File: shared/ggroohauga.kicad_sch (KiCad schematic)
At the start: 6 parts

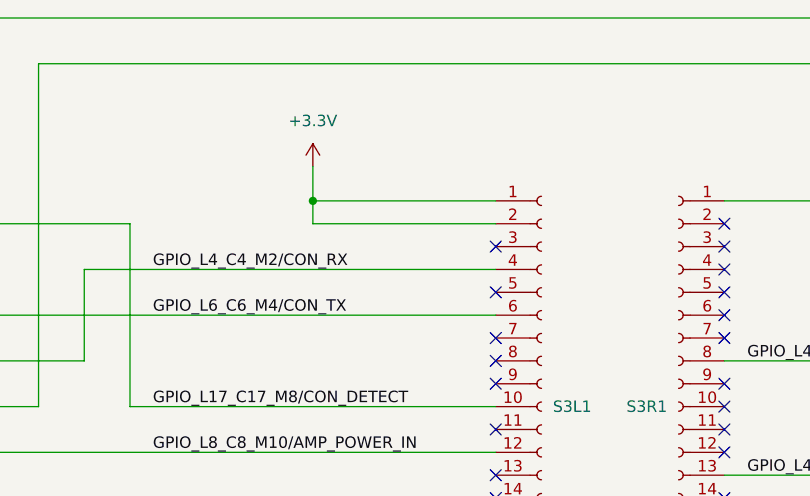
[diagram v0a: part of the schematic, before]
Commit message: Fix compatibility with ESP32-S3-DevKitM-1
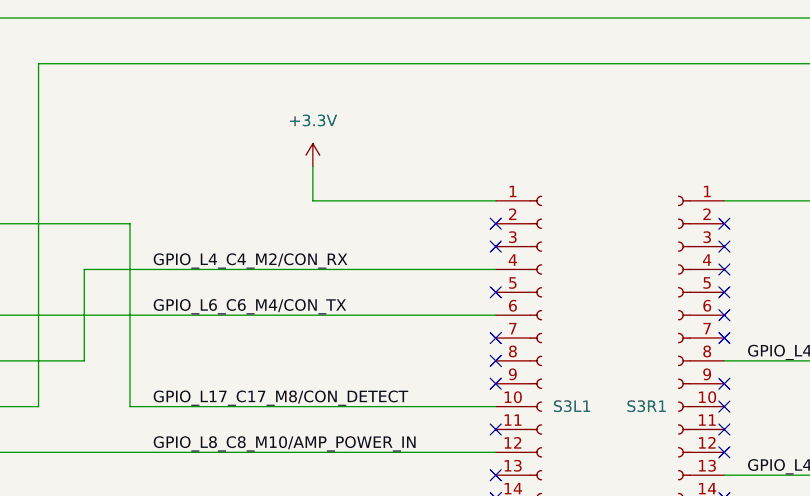
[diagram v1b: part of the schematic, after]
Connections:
- net +3.3V: no longer S3L1.2 (Pin_2)
- no-connect marks 45 -> 46
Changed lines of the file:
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@@
 	(paper "A4")
-	(junction
-		(at 144.78 40.64)
-		(diameter 0)
-		(color 0 0 0 0)
-	)
 	(junction
 		(at 66.04 74.93)
@@
 	)
 	(no_connect
+		(at 165.1 43.18)
+	)
+	(no_connect
 		(at 73.66 129.54)
 	)
@@
 	(wire
 		(pts
-			(xy 165.1 43.18) (xy 144.78 43.18)
-		)
-		(stroke
-			(width 0)
-			(type default)
-		)
-	)
-	(wire
-		(pts
 			(xy 190.5 81.28) (xy 275.59 81.28)
 		)
@@
 		)
 		(stroke
-			(width 0)
-			(type default)
-		)
-	)
-	(wire
-		(pts
-			(xy 144.78 40.64) (xy 144.78 43.18)
-		)
-		(stroke

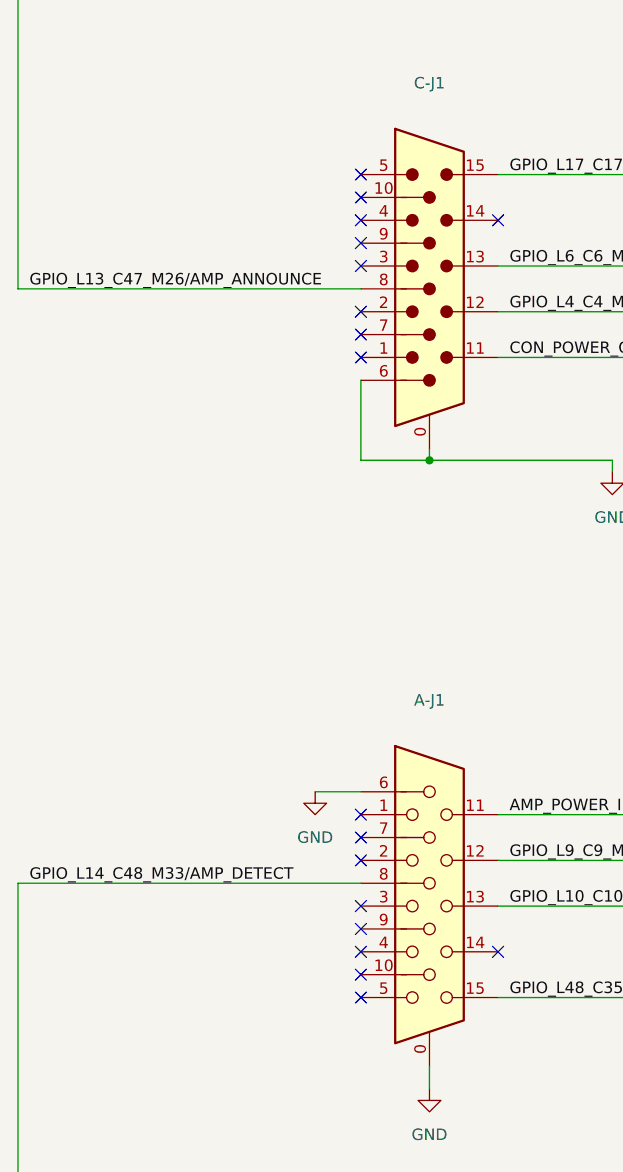
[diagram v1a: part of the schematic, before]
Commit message: Connect audio pins on the bridge PCB
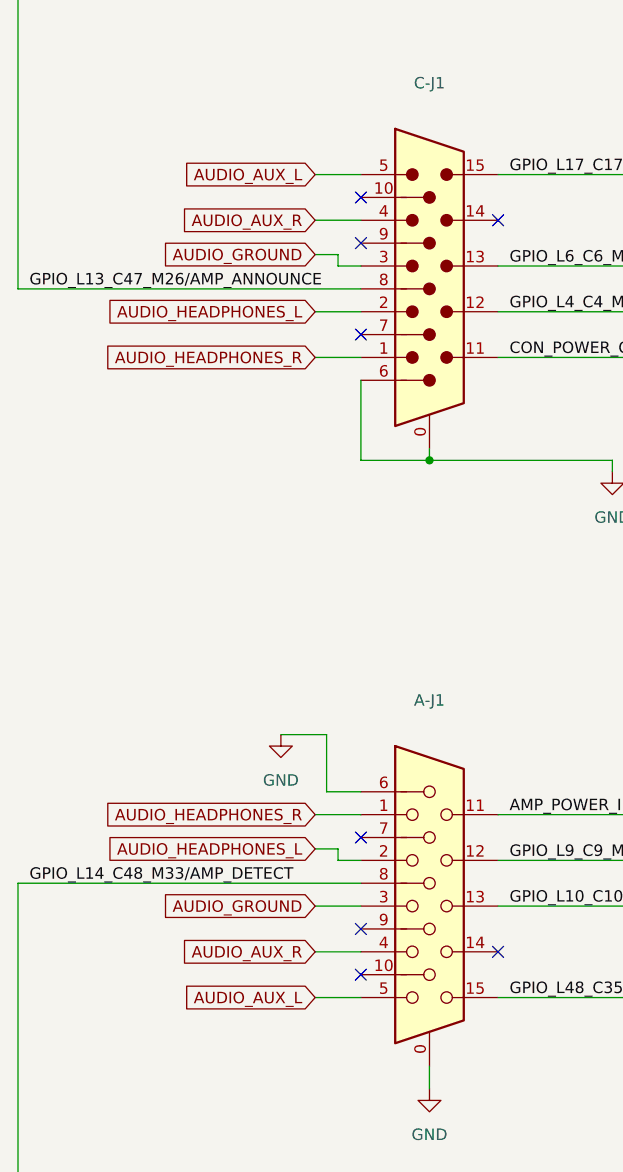
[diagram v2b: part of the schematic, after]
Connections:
- net AUDIO_HEADPHONES_R: now reaches A-J1.1
- net AUDIO_HEADPHONES_R: now also C-J1.1
- net AUDIO_HEADPHONES_L: now reaches A-J1.2
- net AUDIO_HEADPHONES_L: now also C-J1.2
- net AUDIO_GROUND: now reaches A-J1.3
- net AUDIO_GROUND: now also C-J1.3
- net AUDIO_AUX_R: now reaches A-J1.4
- net AUDIO_AUX_R: now also C-J1.4
- net AUDIO_AUX_L: now reaches A-J1.5
- net AUDIO_AUX_L: now also C-J1.5
- no-connect marks 46 -> 36
